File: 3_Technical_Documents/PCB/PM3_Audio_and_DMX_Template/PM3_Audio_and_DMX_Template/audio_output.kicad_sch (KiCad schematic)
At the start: 30 parts, among them U13 OPA2134

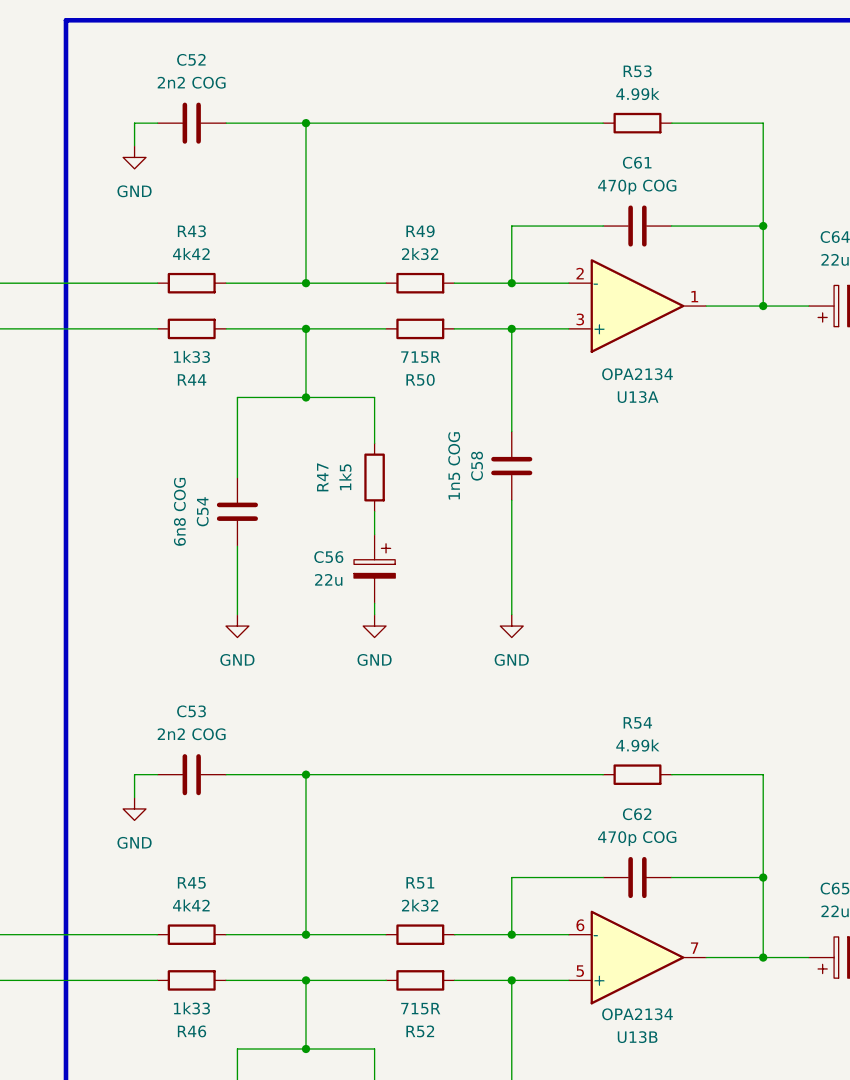
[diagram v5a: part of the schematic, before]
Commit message: schematics, layout and bom updated (to match corrections)
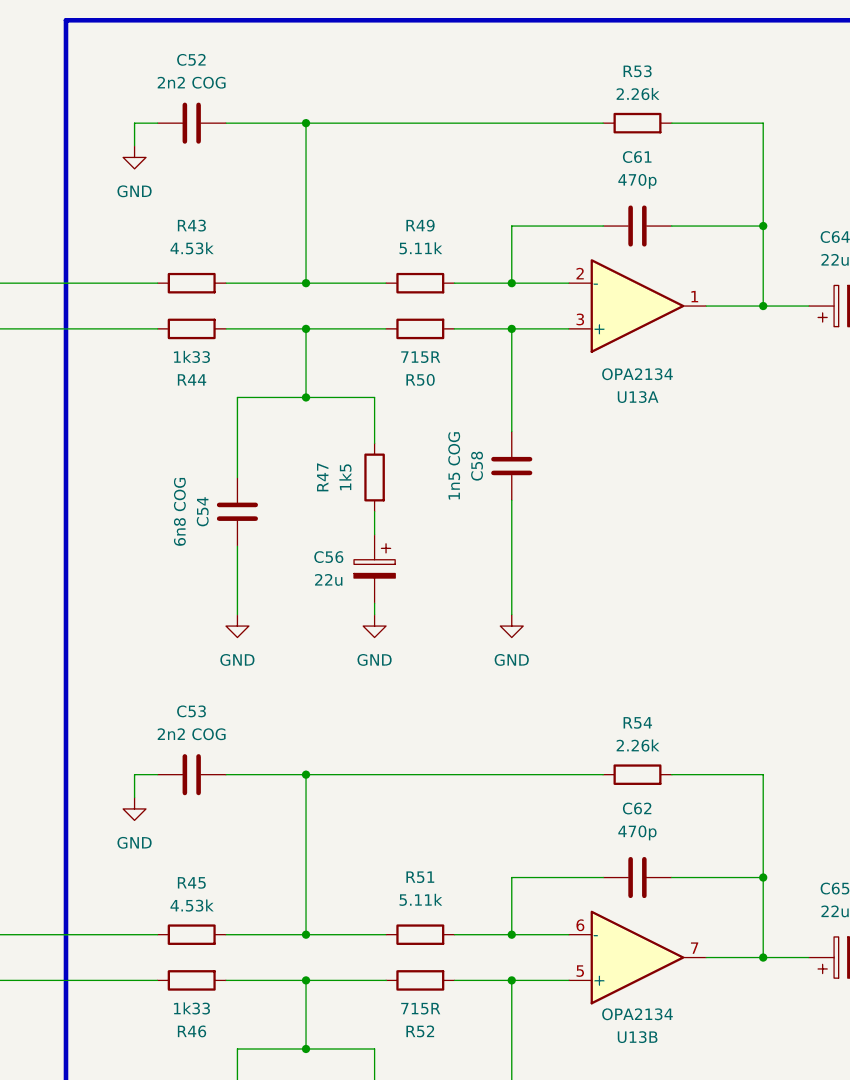
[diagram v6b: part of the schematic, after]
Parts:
- C61, C62: value 470p COG -> 470p
- R43, R45: value 4k42 -> 4.53k; MPN CPF0603F4K99C1 -> (none); Manufacturer TE Connectivity -> (none)
- R49: value 2k32 -> 5.11k; MPN CPF0603F4K99C1 -> (none); Manufacturer TE Connectivity -> (none)
- R51: value 2k32 -> 5.11k; MPN CPF0603F4K99C1 -> (none)
- R53, R54: value 4.99k -> 2.26k; MPN CPF0603F4K99C1 -> (none); Manufacturer TE Connectivity -> (none)
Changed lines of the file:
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@@
 		(fields_autoplaced yes)
 		(property "Reference" "R43"
-			(at 96.52 37.465 90)
+			(at 96.52 36.83 90)
 			(effects
 				(font
@@
 			)
 		)
-		(property "Value" "4k42"
-			(at 96.52 40.005 90)
+		(property "Value" "4.53k"
+			(at 96.52 39.37 90)
 			(effects
 				(font
@@
 			)
 		)
-		(property "Datasheet" "~"
+		(property "Datasheet" ""
 			(at 96.52 43.18 0)
 			(effects
@@
 			)
 		)
-		(property "MPN" "CPF0603F4K99C1"
+		(property "MPN" ""
 			(at 96.52 43.18 90)
 			(effects
@@
 			)
 		)
-		(property "Manufacturer" "TE Connectivity"
+		(property "Manufacturer" ""
 			(at 96.52 43.18 90)
 			(effects
@@
 			)
 		)
-		(property "Value" "4k42"
+		(property "Value" "4.53k"
 			(at 96.52 112.395 90)
 			(effects
@@
 			)
 		)
-		(property "Datasheet" "~"
+		(property "Datasheet" ""
 			(at 96.52 115.57 0)
 			(effects
@@
 			)
 		)
-		(property "MPN" "CPF0603F4K99C1"
+		(property "MPN" ""
 			(at 96.52 115.57 90)
 			(effects
@@
 			)
 		)
-		(property "Manufacturer" "TE Connectivity"
+		(property "Manufacturer" ""
 			(at 96.52 115.57 90)
 			(effects
@@
 		(fields_autoplaced yes)
 		(property "Reference" "C62"
-			(at 146.05 102.235 90)
+			(at 146.05 101.6 90)
 			(effects
 				(font
@@
 			)
 		)
-		(property "Value" "470p COG"
-			(at 146.05 104.775 90)
+		(property "Value" "470p"
+			(at 146.05 104.14 90)
 			(effects
 				(font
@@
 		(fields_autoplaced yes)
 		(property "Reference" "R49"
-			(at 121.92 37.465 90)
+			(at 121.92 36.83 90)
 			(effects
 				(font
@@
 			)
 		)
-		(property "Value" "2k32"
-			(at 121.92 40.005 90)
+		(property "Value" "5.11k"
+			(at 121.92 39.37 90)
 			(effects
 				(font
@@
 			)
 		)
-		(property "Datasheet" "~"
+		(property "Datasheet" ""
 			(at 121.92 43.18 0)
 			(effects
@@
 			)
 		)
-		(property "MPN" "CPF0603F4K99C1"
+		(property "MPN" ""
 			(at 121.92 43.18 90)
 			(effects
@@
 			)
 		)
-		(property "Manufacturer" "TE Connectivity"
+		(property "Manufacturer" ""
 			(at 121.92 43.18 90)
 			(effects
@@
 			)
 		)
-		(property "Value" "4.99k"
+		(property "Value" "2.26k"
 			(at 146.05 22.225 90)
 			(effects
@@
 			)
 		)
-		(property "Datasheet" "~"
+		(property "Datasheet" ""
 			(at 146.05 25.4 0)
 			(effects
@@
 			)
 		)
-		(property "MPN" "CPF0603F4K99C1"
+		(property "MPN" ""
 			(at 146.05 25.4 90)
 			(effects
@@
 			)
 		)
-		(property "Manufacturer" "TE Connectivity"
+		(property "Manufacturer" ""
 			(at 146.05 25.4 90)
 			(effects
@@
 		(fields_autoplaced yes)
 		(property "Reference" "R51"
-			(at 121.92 109.855 90)
+			(at 121.92 109.22 90)
 			(effects
 				(font
@@
 			)
 		)
-		(property "Value" "2k32"
-			(at 121.92 112.395 90)
+		(property "Value" "5.11k"
+			(at 121.92 111.76 90)
 			(effects
 				(font
@@
 			)
 		)
-		(property "Datasheet" "~"
+		(property "Datasheet" ""
 			(at 121.92 115.57 0)
 			(effects
@@
 			)
 		)
-		(property "MPN" "CPF0603F4K99C1"
+		(property "MPN" ""
 			(at 121.92 115.57 90)
 			(effects
@@
 		(fields_autoplaced yes)
 		(property "Reference" "C61"
-			(at 146.05 29.845 90)
+			(at 146.05 29.21 90)
 			(effects
 				(font
@@
 			)
 		)
-		(property "Value" "470p COG"
-			(at 146.05 32.385 90)
+		(property "Value" "470p"
+			(at 146.05 31.75 90)
 			(effects
 				(font
@@
 			)
 		)
-		(property "Value" "4.99k"
+		(property "Value" "2.26k"
 			(at 146.05 94.615 90)
 			(effects
@@
 			)
 		)
-		(property "Datasheet" "~"
+		(property "Datasheet" ""
 			(at 146.05 97.79 0)
 			(effects
@@
 			)
 		)
-		(property "MPN" "CPF0603F4K99C1"
+		(property "MPN" ""
 			(at 146.05 97.79 90)
 			(effects
@@
 			)
 		)
-		(property "Manufacturer" "TE Connectivity"
+		(property "Manufacturer" ""
 			(at 146.05 97.79 90)
 			(effects
